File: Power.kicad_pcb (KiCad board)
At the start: 2 copper layers, 15 x 36 mm, 6 parts, among them P1 CONN_02X10, P2 CONN_01X05, P3 CONN_01X02

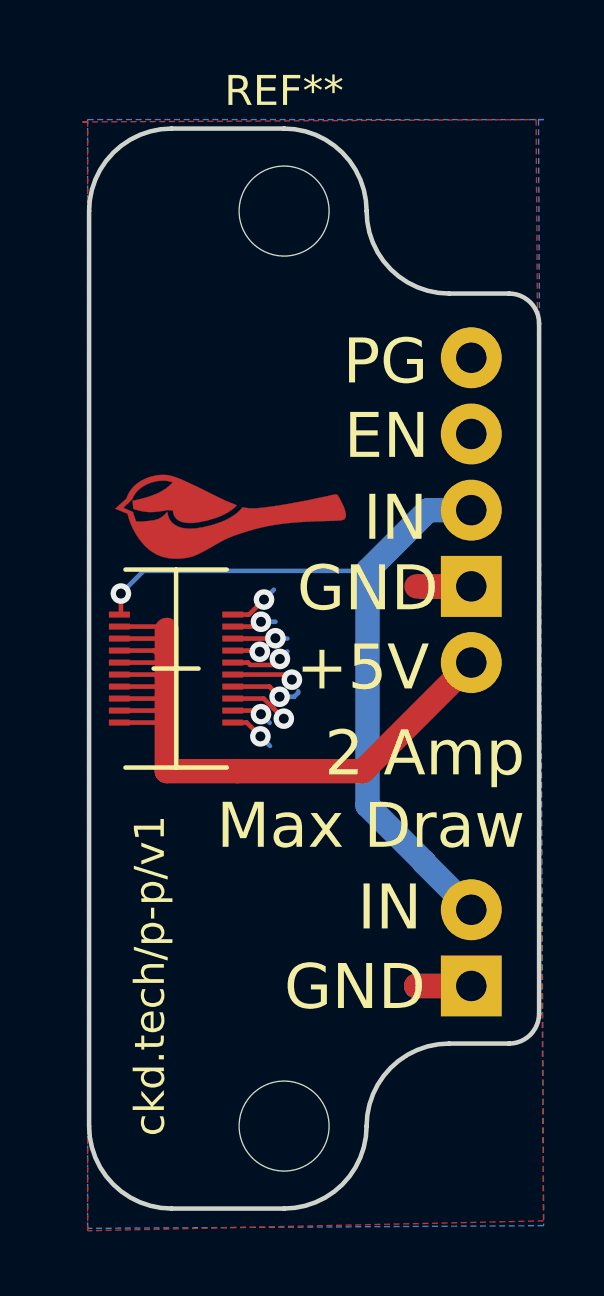
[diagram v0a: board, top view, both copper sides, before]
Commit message: Add voltage divider to pololu power
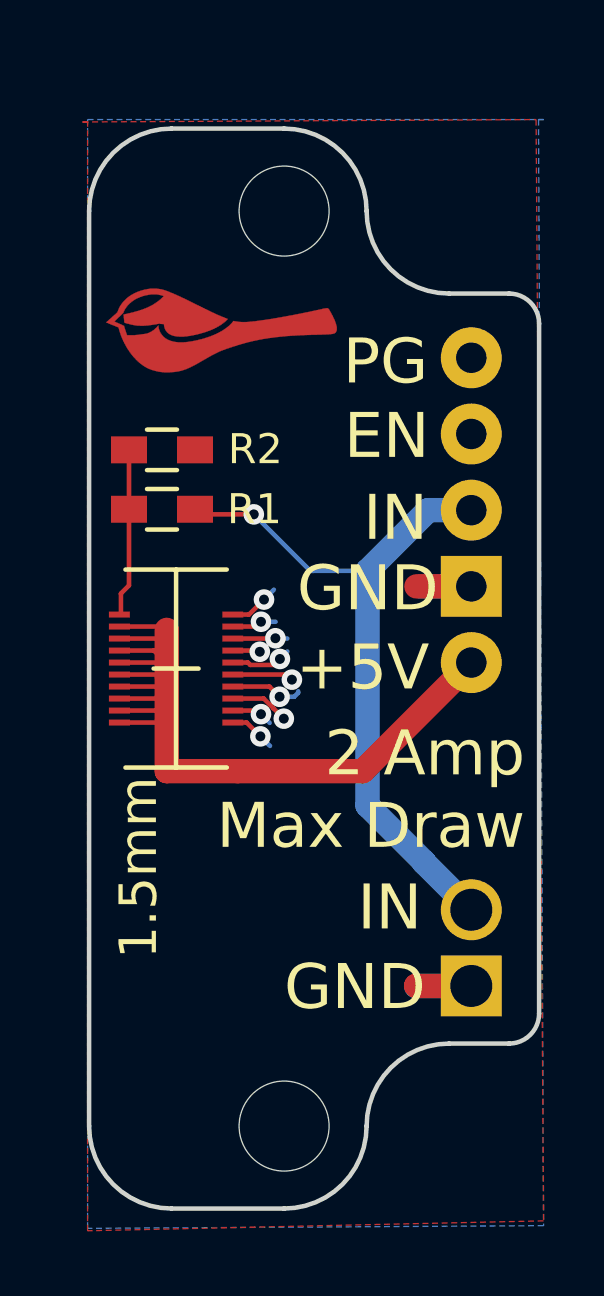
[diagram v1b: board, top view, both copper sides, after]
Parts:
- added R1: 100k, Resistors_SMD:R_0603_HandSoldering, F.Cu at (159.2, 102.7)
- added R2: 10k, Resistors_SMD:R_0603_HandSoldering, F.Cu at (159.2, 100.7)
- moved G*** 6.22 mm to (161.1, 96.7)
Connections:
- P1 pad 19: +BATT -> Net-(P1-Pad19)
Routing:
- net Net-(P1-Pad19): track 0.00 -> 5.62 mm
- net +BATT: track 26.3 -> 23.7 mm
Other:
- board text added: "1.5mm"
- board text added: "ckd.tech/p-p/v2"
- board text removed: "ckd.tech/p-p/v1"
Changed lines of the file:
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@@
-(kicad_pcb (version 4) (host pcbnew "(2015-11-03 BZR 6296)-product")
+(kicad_pcb (version 4) (host pcbnew 4.0.1-stable)
   (general
-    (links 22)
-    (no_connects 11)
+    (links 25)
+    (no_connects 0)
     (area 131.277143 85.19 186.701429 132.68)
     (thickness 1.6)
     (drawings 40)
-    (tracks 90)
+    (tracks 97)
     (zones 0)
-    (modules 6)
-    (nets 6)
+    (modules 8)
+    (nets 7)
   )
   (page USLetter)
@@
   )
   (setup
-    (last_trace_width 0.25)
+    (last_trace_width 0.1524)
     (user_trace_width 0.1524)
     (user_trace_width 0.8128)
@@
     (mod_text_width 0.15)
     (pad_size 2.032 2.032)
-    (pad_drill 1.016)
+    (pad_drill 1.4)
     (pad_to_mask_clearance 0.2)
     (aux_axis_origin 0 0)
@@
   (net 4 "Net-(P2-Pad1)")
   (net 5 "Net-(P2-Pad2)")
+  (net 6 "Net-(P1-Pad19)")
   (net_class Default "This is the default net class."
     (clearance 0.1524)
@@
     (add_net +BATT)
     (add_net GNDPWR)
+    (add_net "Net-(P1-Pad19)")
     (add_net "Net-(P2-Pad1)")
     (add_net "Net-(P2-Pad2)")
@@
     (fp_line (start -1.75 -1.75) (end 1.75 -1.75) (layer F.CrtYd) (width 0.05))
     (fp_line (start -1.75 4.3) (end 1.75 4.3) (layer F.CrtYd) (width 0.05))
-    (pad 1 thru_hole circle (at 0 0) (size 2.032 2.032) (drill 1.016) (layers *.Cu *.Mask F.SilkS)
+    (pad 1 thru_hole circle (at 0 0) (size 2.032 2.032) (drill 1.4) (layers *.Cu *.Mask F.SilkS)
       (net 3 +BATT))
-    (pad 2 thru_hole rect (at 0 2.54) (size 2.032 2.032) (drill 1.016) (layers *.Cu *.Mask F.SilkS)
+    (pad 2 thru_hole rect (at 0 2.54) (size 2.032 2.032) (drill 1.4) (layers *.Cu *.Mask F.SilkS)
       (net 2 GNDPWR))
     (model Pin_Headers.3dshapes/Pin_Header_Straight_1x02.wrl
@@
     (descr "Mounting hole, Befestigungsbohrung, 3mm, No Annular, Kein Restring,")
     (tags "Mounting hole, Befestigungsbohrung, 3mm, No Annular, Kein Restring,")
-    (fp_text reference REF** (at 0 -4.0005) (layer F.SilkS)
+    (fp_text reference REF** (at 0 -4.0005) (layer F.SilkS) hide
       (effects (font (size 1 1) (thickness 0.15)))
     )
@@
       (net 2 GNDPWR))
     (pad 19 smd rect (at -1.89 -1.8) (size 0.7 0.2) (layers F.Cu F.Paste F.Mask)
-      (net 3 +BATT))
+      (net 6 "Net-(P1-Pad19)"))
     (pad 20 smd rect (at 1.89 -1.8) (size 0.7 0.2) (layers F.Cu F.Paste F.Mask)
       (net 2 GNDPWR))
   )
   (module chickadee:chickadee_3mm_fcu (layer F.Cu)
-    (at 161.43 102.94)
+    (at 161.13 96.73)
     (fp_text reference G*** (at 0 0) (layer F.SilkS) hide
       (effects (font (thickness 0.3)))
@@
       (xy -2.200426 -1.477507) (xy -2.158969 -1.476897)) (layer F.Mask) (width 0.01))
   )
-  (gr_text ckd.tech/p-p/v1 (at 158.78 118.24 90) (layer F.SilkS)
-    (effects (font (size 1 1) (thickness 0.15)))
+  (module Resistors_SMD:R_0603_HandSoldering (layer F.Cu)
+    (at 159.18 102.69 180)
+    (descr "Resistor SMD 0603, hand soldering")
+    (tags "resistor 0603")
+    (attr smd)
+    (fp_text reference R1 (at -3.08 0 180) (layer F.SilkS)
+      (effects (font (size 1 1) (thickness 0.15)))
+    )
+    (fp_text value 100k (at 0 1.9 180) (layer F.Fab)
+      (effects (font (size 1 1) (thickness 0.15)))
+    )
+    (fp_line (start -2 -0.8) (end 2 -0.8) (layer F.CrtYd) (width 0.05))
+    (fp_line (start -2 0.8) (end 2 0.8) (layer F.CrtYd) (width 0.05))
+    (fp_line (start -2 -0.8) (end -2 0.8) (layer F.CrtYd) (width 0.05))
+    (fp_line (start 2 -0.8) (end 2 0.8) (layer F.CrtYd) (width 0.05))
+    (fp_line (start 0.5 0.675) (end -0.5 0.675) (layer F.SilkS) (width 0.15))
+    (fp_line (start -0.5 -0.675) (end 0.5 -0.675) (layer F.SilkS) (width 0.15))
+    (pad 1 smd rect (at -1.1 0 180) (size 1.2 0.9) (layers F.Cu F.Paste F.Mask)
+      (net 3 +BATT))
+    (pad 2 smd rect (at 1.1 0 180) (size 1.2 0.9) (layers F.Cu F.Paste F.Mask)
+      (net 6 "Net-(P1-Pad19)"))
+    (model Resistors_SMD.3dshapes/R_0603_HandSoldering.wrl
+      (at (xyz 0 0 0))
+      (scale (xyz 1 1 1))
+      (rotate (xyz 0 0 0))
+    )
+  )
+  (module Resistors_SMD:R_0603_HandSoldering (layer F.Cu)
+    (at 159.18 100.71)
+    (descr "Resistor SMD 0603, hand soldering")
+    (tags "resistor 0603")
+    (attr smd)
+    (fp_text reference R2 (at 3.11 -0.02) (layer F.SilkS)
+      (effects (font (size 1 1) (thickness 0.15)))
+    )
+    (fp_text value 10k (at 0 1.9) (layer F.Fab)
+      (effects (font (size 1 1) (thickness 0.15)))
+    )
+    (fp_line (start -2 -0.8) (end 2 -0.8) (layer F.CrtYd) (width 0.05))
+    (fp_line (start -2 0.8) (end 2 0.8) (layer F.CrtYd) (width 0.05))
+    (fp_line (start -2 -0.8) (end -2 0.8) (layer F.CrtYd) (width 0.05))
+    (fp_line (start 2 -0.8) (end 2 0.8) (layer F.CrtYd) (width 0.05))
+    (fp_line (start 0.5 0.675) (end -0.5 0.675) (layer F.SilkS) (width 0.15))
+    (fp_line (start -0.5 -0.675) (end 0.5 -0.675) (layer F.SilkS) (width 0.15))
+    (pad 1 smd rect (at -1.1 0) (size 1.2 0.9) (layers F.Cu F.Paste F.Mask)
+      (net 6 "Net-(P1-Pad19)"))
+    (pad 2 smd rect (at 1.1 0) (size 1.2 0.9) (layers F.Cu F.Paste F.Mask)
+      (net 2 GNDPWR))
+    (model Resistors_SMD.3dshapes/R_0603_HandSoldering.wrl
+      (at (xyz 0 0 0))
+      (scale (xyz 1 1 1))
+      (rotate (xyz 0 0 0))
+    )
+  )
+  (gr_text 1.5mm (at 158.4 114.64 90) (layer F.SilkS)
+    (effects (font (size 1.25 1.25) (thickness 0.2)))
   )
   (gr_text PG (at 166.63 97.77) (layer B.SilkS)
@@
     (effects (font (size 1.5 1.5) (thickness 0.3)) (justify right))
   )
-  (gr_text ckd.tech/p-p/v1 (at 158.41 107.93 90) (layer B.SilkS)
+  (gr_text ckd.tech/p-p/v2 (at 158.41 107.93 90) (layer B.SilkS)
     (effects (font (size 1.5 1.5) (thickness 0.3)) (justify mirror))
   )
@@
   (segment (start 162.08 106.2) (end 162.58 105.7) (width 0.1524) (layer F.Cu) (net 2))
   (via (at 162.58 105.7) (size 0.6858) (drill 0.3302) (layers F.Cu B.Cu) (net 2))
-  (segment (start 157.81 105.5) (end 157.81 106.15) (width 0.1524) (layer F.Cu) (net 3))
-  (segment (start 157.81 106.15) (end 157.76 106.2) (width 0.1524) (layer F.Cu) (net 3))
-  (segment (start 166.03 104.74316) (end 158.56684 104.74316) (width 0.1524) (layer B.Cu) (net 3))
-  (segment (start 158.56684 104.74316) (end 157.81 105.5) (width 0.1524) (layer B.Cu) (net 3))
-  (via (at 157.81 105.5) (size 0.6858) (drill 0.3302) (layers F.Cu B.Cu) (net 3))
+  (segment (start 162.24 102.86) (end 160.45 102.86) (width 0.1524) (layer F.Cu) (net 3))
+  (segment (start 160.45 102.86) (end 160.28 102.69) (width 0.1524) (layer F.Cu) (net 3))
+  (segment (start 164.21316 104.74316) (end 164.12316 104.74316) (width 0.1524) (layer B.Cu) (net 3))
+  (segment (start 164.12316 104.74316) (end 162.24 102.86) (width 0.1524) (layer B.Cu) (net 3))
+  (via (at 162.24 102.86) (size 0.6858) (drill 0.3302) (layers F.Cu B.Cu) (net 3))
+  (segment (start 160.31 102.72) (end 160.28 102.69) (width 0.1524) (layer F.Cu) (net 3))
+  (segment (start 166.03 104.74316) (end 164.21316 104.74316) (width 0.1524) (layer B.Cu) (net 3))
+  (segment (start 168.05316 102.72) (end 169.49 102.72) (width 0.8128) (layer B.Cu) (net 3))
+  (segment (start 169.49 116.04) (end 167.915199 114.465199) (width 0.8128) (layer B.Cu) (net 3))
   (segment (start 166.03 112.56) (end 166.03 104.74316) (width 0.8128) (layer B.Cu) (net 3))
   (segment (start 166.03 104.74316) (end 168.05316 102.72) (width 0.8128) (layer B.Cu) (net 3))
-  (segment (start 168.05316 102.72) (end 169.49 102.72) (width 0.8128) (layer B.Cu) (net 3))
   (segment (start 167.915199 114.445199) (end 166.03 112.56) (width 0.8128) (layer B.Cu) (net 3))
-  (segment (start 169.49 116.04) (end 167.915199 114.465199) (width 0.8128) (layer B.Cu) (net 3))
   (segment (start 167.915199 114.465199) (end 167.915199 114.445199) (width 0.8128) (layer B.Cu) (net 3))
+  (segment (start 158.08 102.69) (end 158.08 105.23) (width 0.1524) (layer F.Cu) (net 6))
+  (segment (start 158.08 105.23) (end 157.81 105.5) (width 0.1524) (layer F.Cu) (net 6))
+  (segment (start 158.08 100.71) (end 158.08 102.69) (width 0.1524) (layer F.Cu) (net 6))
+  (segment (start 157.81 105.5) (end 157.81 106.15) (width 0.1524) (layer F.Cu) (net 6))
+  (segment (start 157.81 106.15) (end 157.76 106.2) (width 0.1524) (layer F.Cu) (net 6))
   (zone (net 2) (net_name GNDPWR) (layer F.Cu) (hatch edge 0.508)
     (connect_pads (clearance 0.5))
@@
       )
     )
+  )
+  (zone (net 0) (net_name "") (layer F.Cu) (hatch edge 0.508)
+    (connect_pads (clearance 0.5))
+    (min_thickness 0.254)
+    (keepout (tracks allowed) (vias allowed) (copperpour not_allowed))
+    (fill yes (arc_segments 16) (thermal_gap 0.508) (thermal_bridge_width 0.508))
+    (polygon
+      (pts
+        (xy 161.01 105.85) (xy 162.07 105.9) (xy 161.96 110.14) (xy 160.92 110.17) (xy 161.06 105.9)
+      )
+    )

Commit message: v3 of pololu power. Moved pololu headers to the board edge, centered it to fit narrow standoffs, switched 5v traces to outside to hopefully strengthen the solder joint, and make annular ring of power holes larger. Thanks to Rothany Hin for breaking v2s swiftly.
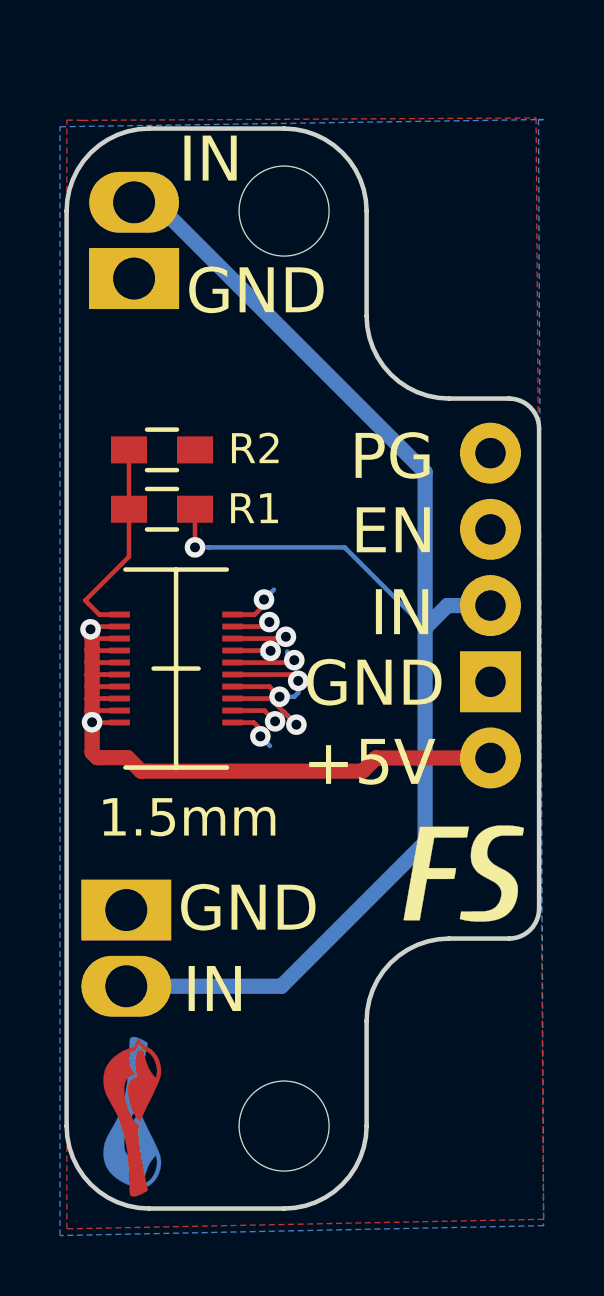
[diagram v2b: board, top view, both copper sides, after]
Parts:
- removed the G*** at (161.1, 96.7)
- added G***: LOGO, flightstack:fs-4mm, B.Cu at (169.2, 114.8)
- added G***: LOGO, chickadee:chickadee_2mm_fcu, B.Cu at (158.2, 122.9)
- added G***: LOGO, chickadee:chickadee_2mm_fcu, F.Cu at (158.2, 122.9)
- added G***: LOGO, flightstack:fs-4mm, F.Cu at (169.2, 114.8)
- added P4: CONN_01X02, pin-headers:16awg_Pin_Header_Straight_1x02, F.Cu at (158.0, 116.0)
- P3: footprint Pin_Headers:Pin_Header_Straight_1x02 -> pin-headers:16awg_Pin_Header_Straight_1x02
- moved P3 23.9 mm to (158.2, 95.0), turned to 180 degrees
- moved P2 3.24 mm to (170.1, 100.8)
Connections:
- P3 pad 1: +BATT -> GNDPWR
- P3 pad 2: GNDPWR -> +BATT
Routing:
- net +BATT: track 23.7 -> 50.3 mm
- net +5V: track 31.3 -> 26.2 mm, vias 0 -> 2
- net GNDPWR: track 25.3 -> 20.8 mm
- net Net-(P1-Pad19): track 5.62 -> 6.96 mm
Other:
- board size 15 x 36 mm -> 15.8 x 36 mm
- net class Default: via_dia 0.6 -> 0.6858; via_drill 0.4 -> 0.3302
- net class Expansion Power: via_dia 0.6 -> 0.6858; via_drill 0.4 -> 0.3302
- board text added: "ckd.tech/p-p/v3"
- board text removed: "2 Amp Max Draw"
- board text removed: "ckd.tech/p-p/v2"
